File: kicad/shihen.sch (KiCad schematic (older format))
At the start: 51 parts, among them J1 Conn_01x06, J4 USBChargingBoard, Q1 Si1308EDL_NMOS_GSD, Q2 IRLML2502TR(SOT-23, Q_PMOS_GS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, SW1 SW_Push, U1 TPL5110, U2 ESP-12E, U3 ws_epaper_24pin, U4 xc6206p332mr(SOT-23), U5 PCF8563T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

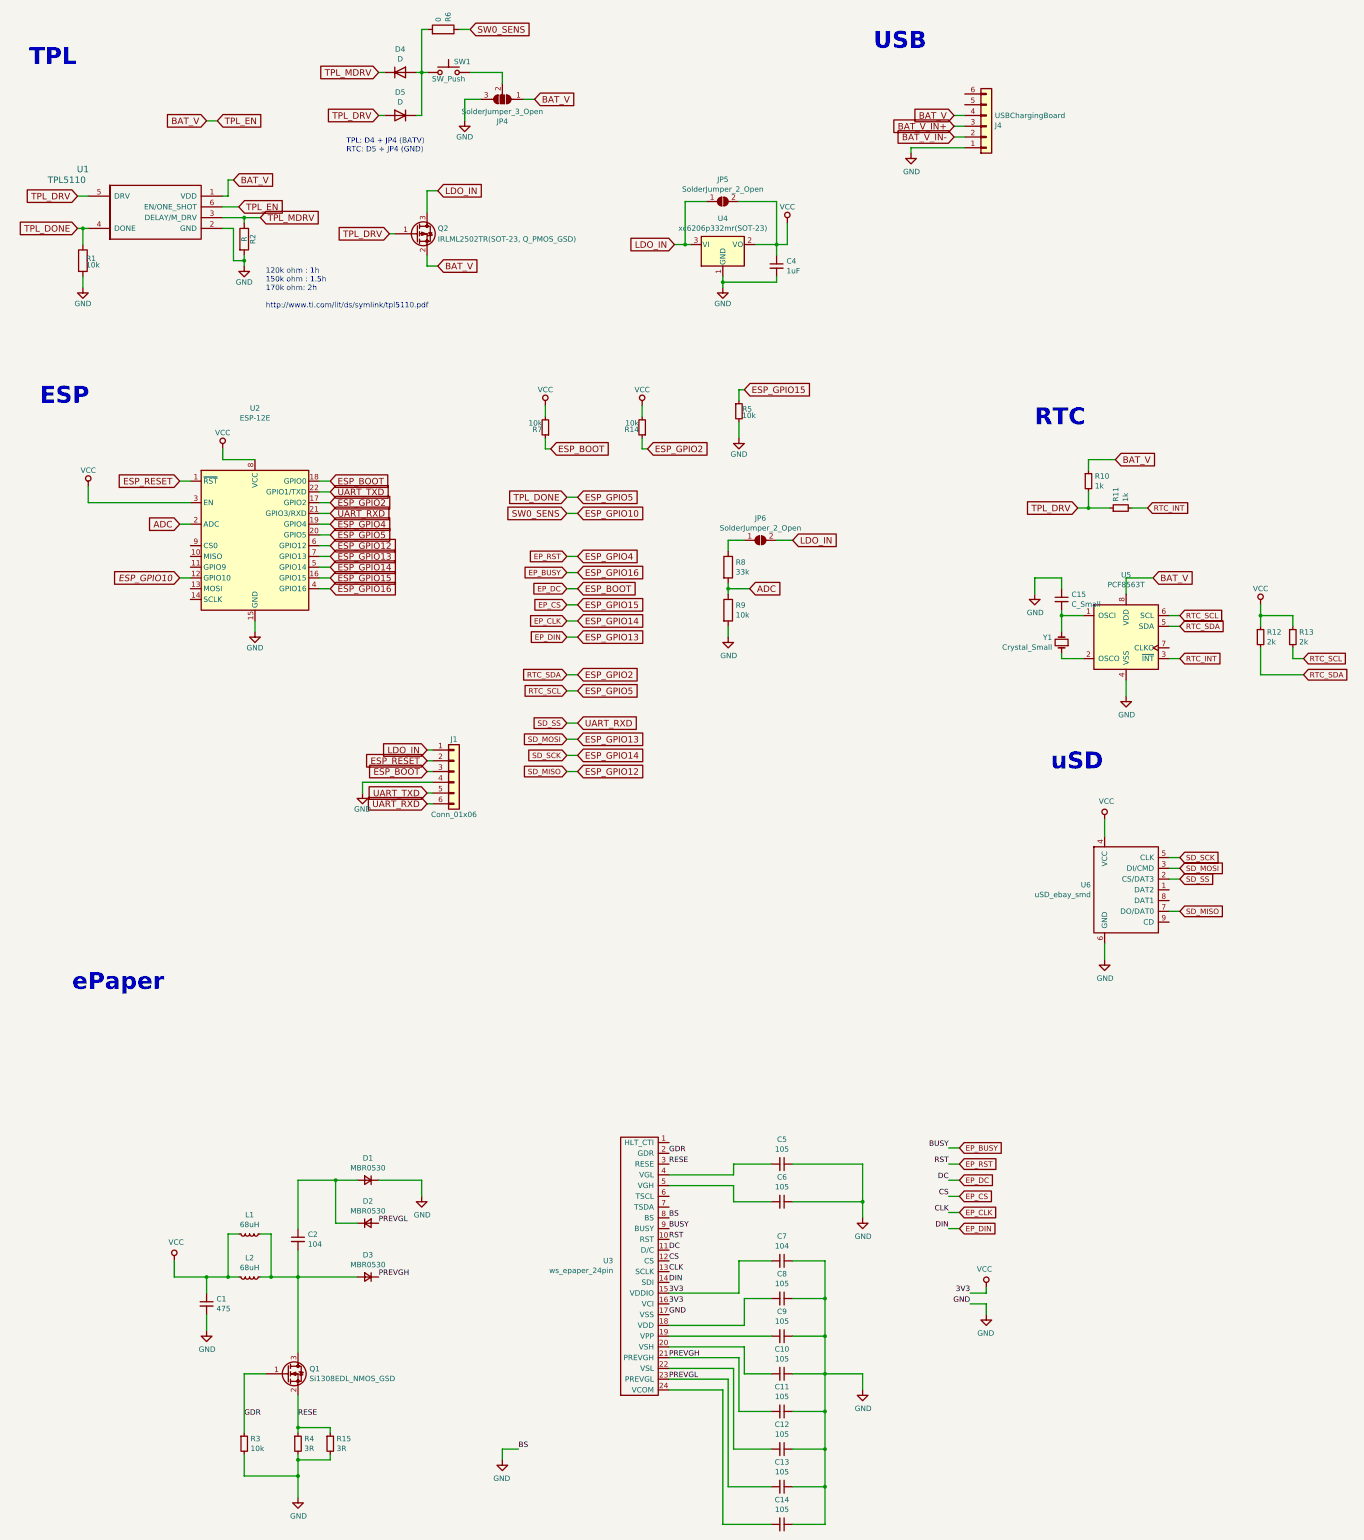
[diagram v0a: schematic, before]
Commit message: Modify schemas - Add MPN(Fusion PCB's part number) as an attribute for PCBA - Fix some wrong constants
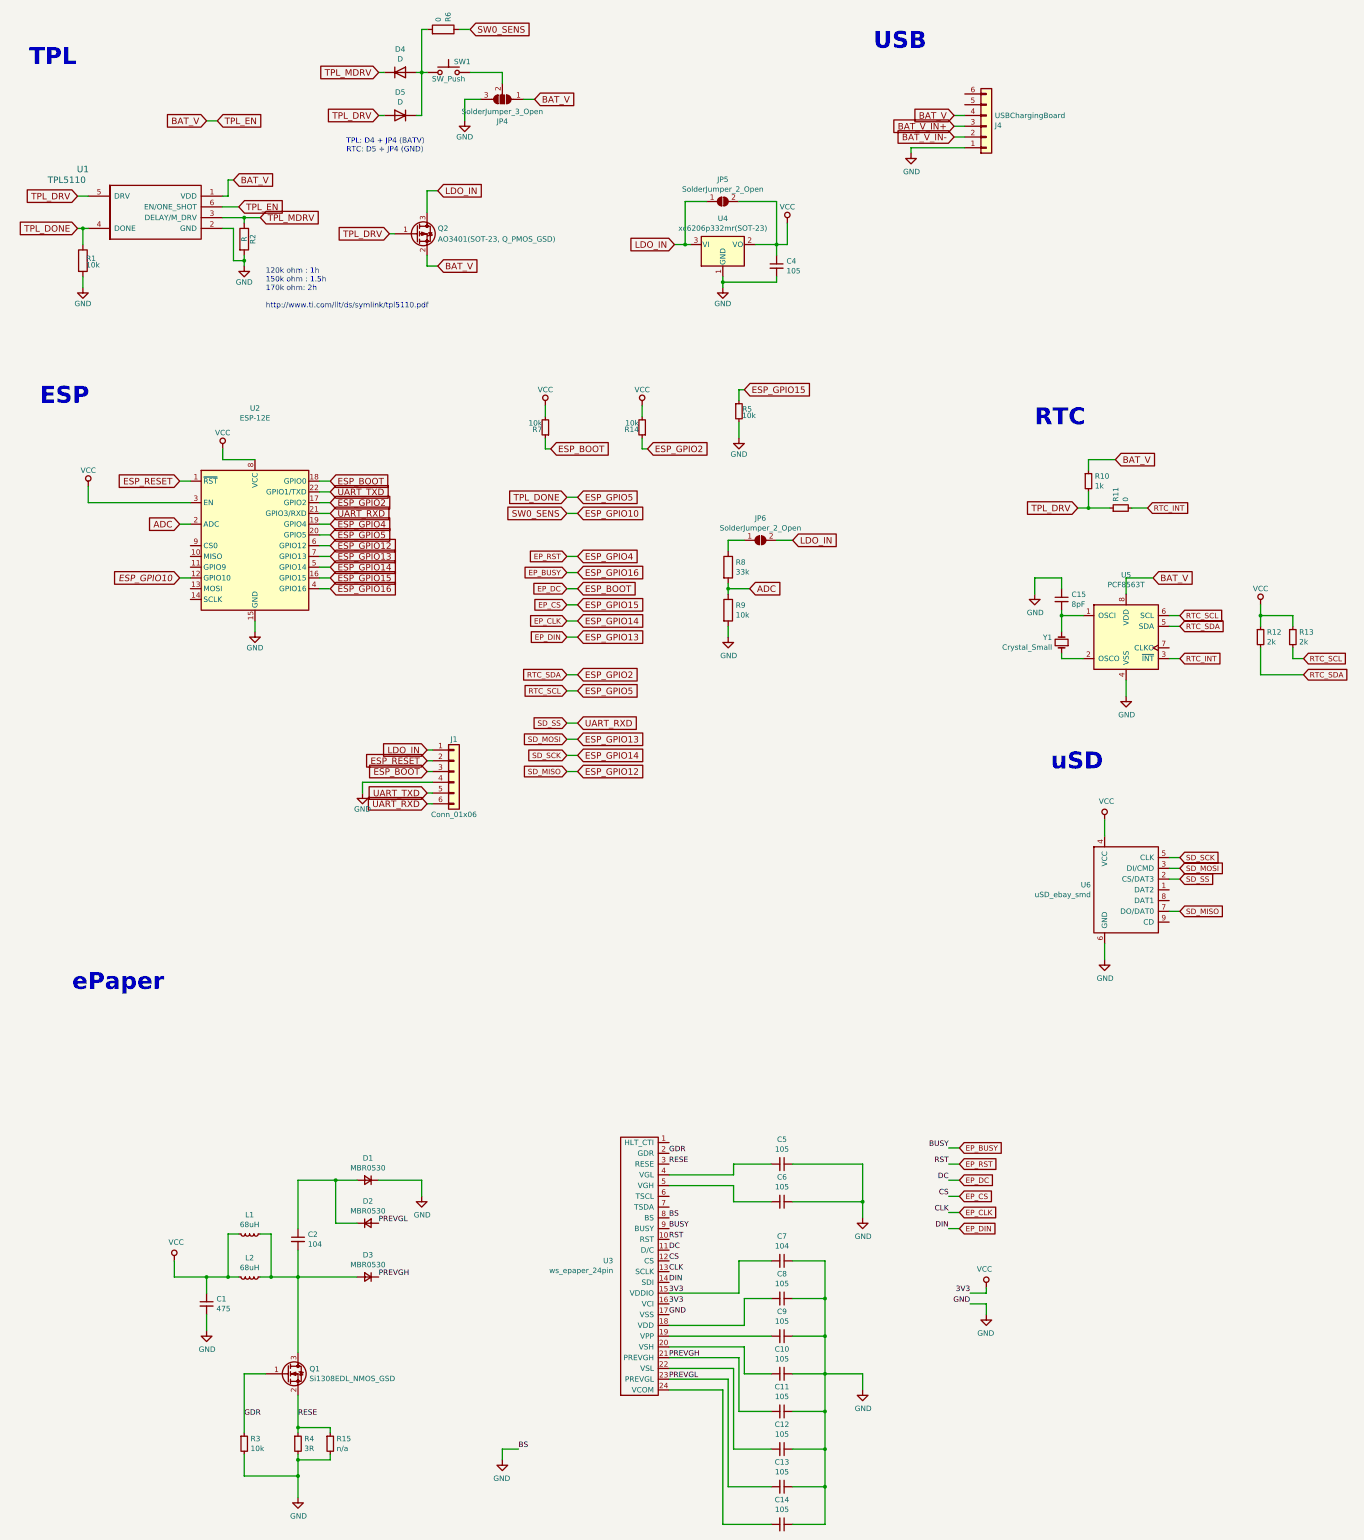
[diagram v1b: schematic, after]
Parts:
- C1: MPN (none) -> CC0805KKX5R8BB475
- C10, C11, C12, C13, C14, C5, C6, C8, C9: MPN (none) -> CC0805KKX7R8BB105
- C15: value C_Small -> 8pF; MPN (none) -> 0805CG8R0C500NT
- C2, C7: MPN (none) -> C0805X104K101T
- C4: value 1uF -> 105; MPN (none) -> CC0805KKX7R8BB105
- D1, D2, D3: MPN (none) -> MBR0530
- D4, D5: MPN (none) -> LL4148ST
- L2: MPN (none) -> NLCV32T-680K-PF
- Q1: MPN_disabled (none) -> SI1308EDL-T1-GE3
- Q2: value IRLML2502TR(SOT-23, Q_PMOS_GSD) -> AO3401(SOT-23, Q_PMOS_GSD); MPN (none) -> CJ2305
- R1, R14, R3, R5, R7, R9: MPN (none) -> RC0805FR-0710KL
- R10: MPN (none) -> RC0805JR-071KL
- R11: value 1k -> 0; MPN (none) -> RC0805FR-070RL
- R15: value 3R -> n/a
- R4: MPN (none) -> 0805W8F300KT5E
- R6: MPN (none) -> RC0805FR-070RL
- R8: MPN (none) -> RC0805FR-0733KL
- U2: MPN (none) -> ESP-12E
- U3: MPN (none) -> FH12A-24S-0.5SH(55)
- U4: MPN (none) -> XC6206P332MR-G
- U5: MPN_disabled (none) -> PCF8563T/5,518
- U6: MPN (none) -> TF-01
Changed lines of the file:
@@
 F 2 "Capacitor_SMD:C_0805_2012Metric_Pad1.15x1.40mm_HandSolder" H 8500 11650 50  0001 C CNN
 F 3 "~" H 8500 11650 50  0001 C CNN
+F 4 "CC0805KKX7R8BB105" H 0   0   50  0001 C CNN "MPN"
 	1    8500 11650
 	0    1    1    0
@@
 F 2 "Capacitor_SMD:C_0805_2012Metric_Pad1.15x1.40mm_HandSolder" H 8500 12000 50  0001 C CNN
 F 3 "~" H 8500 12000 50  0001 C CNN
+F 4 "CC0805KKX7R8BB105" H 0   0   50  0001 C CNN "MPN"
 	1    8500 12000
 	0    1    1    0
@@
 F 2 "Capacitor_SMD:C_0805_2012Metric_Pad1.15x1.40mm_HandSolder" H 8500 12550 50  0001 C CNN
 F 3 "~" H 8500 12550 50  0001 C CNN
+F 4 "C0805X104K101T" H 0   0   50  0001 C CNN "MPN"
 	1    8500 12550
 	0    1    1    0
@@
 F 2 "Capacitor_SMD:C_0805_2012Metric_Pad1.15x1.40mm_HandSolder" H 8500 12900 50  0001 C CNN
 F 3 "~" H 8500 12900 50  0001 C CNN
+F 4 "CC0805KKX7R8BB105" H 0   0   50  0001 C CNN "MPN"
 	1    8500 12900
 	0    1    1    0
@@
 F 2 "Capacitor_SMD:C_0805_2012Metric_Pad1.15x1.40mm_HandSolder" H 8500 13250 50  0001 C CNN
 F 3 "~" H 8500 13250 50  0001 C CNN
+F 4 "CC0805KKX7R8BB105" H 0   0   50  0001 C CNN "MPN"
 	1    8500 13250
 	0    1    1    0
@@
 F 2 "Capacitor_SMD:C_0805_2012Metric_Pad1.15x1.40mm_HandSolder" H 8500 13600 50  0001 C CNN
 F 3 "~" H 8500 13600 50  0001 C CNN
+F 4 "CC0805KKX7R8BB105" H 0   0   50  0001 C CNN "MPN"
 	1    8500 13600
 	0    1    1    0
@@
 F 2 "Capacitor_SMD:C_0805_2012Metric_Pad1.15x1.40mm_HandSolder" H 8500 13950 50  0001 C CNN
 F 3 "~" H 8500 13950 50  0001 C CNN
+F 4 "CC0805KKX7R8BB105" H 0   0   50  0001 C CNN "MPN"
 	1    8500 13950
 	0    1    1    0
@@
 F 2 "Capacitor_SMD:C_0805_2012Metric_Pad1.15x1.40mm_HandSolder" H 8500 14300 50  0001 C CNN
 F 3 "~" H 8500 14300 50  0001 C CNN
+F 4 "CC0805KKX7R8BB105" H 0   0   50  0001 C CNN "MPN"
 	1    8500 14300
 	0    1    1    0
@@
 F 2 "Capacitor_SMD:C_0805_2012Metric_Pad1.15x1.40mm_HandSolder" H 8500 14650 50  0001 C CNN
 F 3 "~" H 8500 14650 50  0001 C CNN
+F 4 "CC0805KKX7R8BB105" H 0   0   50  0001 C CNN "MPN"
 	1    8500 14650
 	0    1    1    0
@@
 F 2 "Capacitor_SMD:C_0805_2012Metric_Pad1.15x1.40mm_HandSolder" H 8500 15000 50  0001 C CNN
 F 3 "~" H 8500 15000 50  0001 C CNN
+F 4 "CC0805KKX7R8BB105" H 0   0   50  0001 C CNN "MPN"
 	1    8500 15000
 	0    1    1    0
@@
 F 2 "Connector_FFC-FPC:Hirose_FH12-24S-0.5SH_1x24-1MP_P0.50mm_Horizontal_reverse" H 7350 11250 50  0001 C CNN
 F 3 "" H 7350 11250 50  0001 C CNN
+F 4 "FH12A-24S-0.5SH(55)" H 0   0   50  0001 C CNN "MPN"
 	1    7350 11250
 	-1   0    0    -1
@@
 F 2 "Diode_SMD:D_SOD-123" V 4650 11800 50  0001 C CNN
 F 3 "~" V 4650 11800 50  0001 C CNN
+F 4 "MBR0530" H 0   0   50  0001 C CNN "MPN"
 	1    4650 11800
 	-1   0    0    1
@@
 F 2 "Diode_SMD:D_SOD-123" V 4650 12200 50  0001 C CNN
 F 3 "~" V 4650 12200 50  0001 C CNN
+F 4 "MBR0530" H 0   0   50  0001 C CNN "MPN"
 	1    4650 12200
 	1    0    0    1
@@
 F 2 "Diode_SMD:D_SOD-123" V 4650 12700 50  0001 C CNN
 F 3 "~" V 4650 12700 50  0001 C CNN
+F 4 "MBR0530" H 0   0   50  0001 C CNN "MPN"
 	1    4650 12700
 	-1   0    0    1
@@
 F 2 "Capacitor_SMD:C_0805_2012Metric_Pad1.15x1.40mm_HandSolder" H 4000 12350 50  0001 C CNN
 F 3 "~" H 4000 12350 50  0001 C CNN
+F 4 "C0805X104K101T" H 0   0   50  0001 C CNN "MPN"
 	1    4000 12350
 	1    0    0    -1
@@
 F 2 "Inductor_SMD:L_1206_3216Metric_Pad1.42x1.75mm_HandSolder" H 3550 12700 50  0001 C CNN
 F 3 "~" H 3550 12700 50  0001 C CNN
+F 4 "NLCV32T-680K-PF" H 0   0   50  0001 C CNN "MPN"
 	1    3550 12700
 	0    1    1    0
@@
 F 2 "Capacitor_SMD:C_0805_2012Metric_Pad1.15x1.40mm_HandSolder" H 3150 12950 50  0001 C CNN
 F 3 "~" H 3150 12950 50  0001 C CNN
+F 4 "CC0805KKX5R8BB475" H 0   0   50  0001 C CNN "MPN"
 	1    3150 12950
 	1    0    0    -1
@@
 F 2 "Package_TO_SOT_SMD:SOT-323_SC-70_Handsoldering" H 4100 13700 50  0001 C CNN
 F 3 "~" H 3900 13600 50  0001 C CNN
+F 4 "SI1308EDL-T1-GE3" H 0   0   50  0001 C CNN "MPN_disabled"
 	1    3900 13600
 	1    0    0    -1
@@
 F 2 "Resistor_SMD:R_0805_2012Metric" H 4000 14250 50  0001 C CNN
 F 3 "~" H 4000 14250 50  0001 C CNN
+F 4 "0805W8F300KT5E" H 0   0   50  0001 C CNN "MPN"
 	1    4000 14250
 	1    0    0    -1
@@
 F 2 "Resistor_SMD:R_0805_2012Metric" H 3500 14250 50  0001 C CNN
 F 3 "~" H 3500 14250 50  0001 C CNN
+F 4 "RC0805FR-0710KL" H 0   0   50  0001 C CNN "MPN"
 	1    3500 14250
 	1    0    0    -1
@@
 F 2 "Resistor_SMD:R_0805_2012Metric" H 8100 4650 50  0001 C CNN
 F 3 "" H 8100 4650 50  0001 C CNN
+F 4 "RC0805FR-0710KL" H 0   0   50  0001 C CNN "MPN"
 	1    8100 4650
 	1    0    0    -1
@@
 F 2 "Resistor_SMD:R_0805_2012Metric" H 6300 4800 50  0001 C CNN
 F 3 "" H 6300 4800 50  0001 C CNN
+F 4 "RC0805FR-0710KL" H 0   0   50  0001 C CNN "MPN"
 	1    6300 4800
 	-1   0    0    1
@@
 P 5100 3000
 F 0 "Q2" H 5300 3050 50  0000 L CNN
-F 1 "IRLML2502TR(SOT-23, Q_PMOS_GSD)" H 5300 2950 50  0000 L CNN
+F 1 "AO3401(SOT-23, Q_PMOS_GSD)" H 5300 2950 50  0000 L CNN
 F 2 "Package_TO_SOT_SMD:SOT-23_Handsoldering" H 5300 3100 50  0001 C CNN
 F 3 "" H 5100 3000 50  0001 C CNN
+F 4 "CJ2305" H 0   0   50  0001 C CNN "MPN"
 	1    5100 3000
 	1    0    0    -1
@@
 F 2 "Resistor_SMD:R_0805_2012Metric" H 2000 3250 50  0001 C CNN
 F 3 "" H 2000 3250 50  0001 C CNN
+F 4 "RC0805FR-0710KL" H 0   0   50  0001 C CNN "MPN"
 	1    2000 3250
 	1    0    0    -1
@@
 P 8450 3300
 F 0 "C4" H 8542 3346 50  0000 L CNN
-F 1 "1uF" H 8542 3255 50  0000 L CNN
+F 1 "105" H 8542 3255 50  0000 L CNN
 F 2 "Capacitor_SMD:C_0805_2012Metric_Pad1.15x1.40mm_HandSolder" H 8450 3300 50  0001 C CNN
 F 3 "~" H 8450 3300 50  0001 C CNN
+F 4 "CC0805KKX7R8BB105" H 0   0   50  0001 C CNN "MPN"
 	1    8450 3300
 	1    0    0    -1
@@
 F 2 "Package_TO_SOT_SMD:SOT-23_Handsoldering" H 7950 3300 50  0001 C CNN
 F 3 "http://www.diodes.com/datasheets/AP1117.pdf" H 8050 2850 50  0001 C CNN
+F 4 "XC6206P332MR-G" H 0   0   50  0001 C CNN "MPN"
 	1    7950 3100
 	1    0    0    -1
@@
 F 2 "lib_ext:ESP-12E" H 3600 6150 50  0001 C CNN
 F 3 "http://wiki.ai-thinker.com/_media/esp8266/docs/aithinker_esp_12f_datasheet_en.pdf" H 3250 6200 50  0001 C CNN
+F 4 "ESP-12E" H 3600 5900 50  0001 C CNN "MPN"
 	1    3600 5900
 	1    0    0    -1
@@
 F 2 "Resistor_SMD:R_0805_2012Metric" V 7930 6100 50  0001 C CNN
 F 3 "~" H 8000 6100 50  0001 C CNN
+F 4 "RC0805FR-0733KL" H 0   0   50  0001 C CNN "MPN"
 	1    8000 6100
 	1    0    0    -1
@@
 F 2 "Resistor_SMD:R_0805_2012Metric" V 7930 6500 50  0001 C CNN
 F 3 "~" H 8000 6500 50  0001 C CNN
+F 4 "RC0805FR-0710KL" H 0   0   50  0001 C CNN "MPN"
 	1    8000 6500
 	1    0    0    -1
@@
 F 2 "Diode_SMD:D_1206_3216Metric_Pad1.42x1.75mm_HandSolder" H 4950 1500 50  0001 C CNN
 F 3 "~" H 4950 1500 50  0001 C CNN
+F 4 "LL4148ST" H 0   0   50  0001 C CNN "MPN"
 	1    4950 1500
 	1    0    0    -1
@@
 F 2 "Resistor_SMD:R_0805_2012Metric" V 5280 1100 50  0001 C CNN
 F 3 "~" H 5350 1100 50  0001 C CNN
+F 4 "RC0805FR-070RL" H 0   0   50  0001 C CNN "MPN"
 	1    5350 1100
 	0    1    -1   0
@@
 F 2 "Package_SO:SOIC-8_3.9x4.9mm_P1.27mm" H 11700 6750 50  0001 C CNN
 F 3 "http://www.nxp.com/documents/data_sheet/PCF8563.pdf" H 11700 6750 50  0001 C CNN
+F 4 "PCF8563T/5,518" H 0   0   50  0001 C CNN "MPN_disabled"
 	1    11700 6750
 	1    0    0    -1
@@
 P 11100 6400
 F 0 "C15" H 11192 6446 50  0000 L CNN
-F 1 "C_Small" H 11192 6355 50  0000 L CNN
+F 1 "8pF" H 11192 6355 50  0000 L CNN
 F 2 "Capacitor_SMD:C_0805_2012Metric_Pad1.15x1.40mm_HandSolder" H 11100 6400 50  0001 C CNN
 F 3 "~" H 11100 6400 50  0001 C CNN
+F 4 "0805CG8R0C500NT" H 0   0   50  0001 C CNN "MPN"
 	1    11100 6400
 	1    0    0    -1
@@
 F 2 "Resistor_SMD:R_0805_2012Metric" H 11350 5300 50  0001 C CNN
 F 3 "~" H 11350 5300 50  0001 C CNN
+F 4 "RC0805JR-071KL" H 0   0   50  0001 C CNN "MPN"
 	1    11350 5300
 	1    0    0    -1
@@
 P 11650 5550
 F 0 "R11" H 11709 5596 50  0000 L CNN
-F 1 "1k" H 11709 5505 50  0000 L CNN
+F 1 "0" H 11709 5505 50  0000 L CNN
 F 2 "Resistor_SMD:R_0805_2012Metric" H 11650 5550 50  0001 C CNN
 F 3 "~" H 11650 5550 50  0001 C CNN
+F 4 "RC0805FR-070RL" H 0   0   50  0001 C CNN "MPN"
 	1    11650 5550
 	0    -1   -1   0
@@
 F 2 "Diode_SMD:D_1206_3216Metric_Pad1.42x1.75mm_HandSolder" H 4950 1900 50  0001 C CNN
 F 3 "~" H 4950 1900 50  0001 C CNN
+F 4 "LL4148ST" H 0   0   50  0001 C CNN "MPN"
 	1    4950 1900
 	-1   0    0    -1
@@
 F 2 "Resistor_SMD:R_0805_2012Metric" H 7200 4800 50  0001 C CNN
 F 3 "" H 7200 4800 50  0001 C CNN
+F 4 "RC0805FR-0710KL" H 0   0   50  0001 C CNN "MPN"
 	1    7200 4800
 	-1   0    0    1
@@
 P 4300 14250
 F 0 "R15" H 4359 14296 50  0000 L CNN
-F 1 "3R" H 4359 14205 50  0000 L CNN
+F 1 "n/a" H 4359 14205 50  0000 L CNN
 F 2 "Resistor_SMD:R_0805_2012Metric" H 4300 14250 50  0001 C CNN
 F 3 "~" H 4300 14250 50  0001 C CNN
+F 4 "" H 0   0   50  0001 C CNN "MPN"
 	1    4300 14250
 	1    0    0    -1
@@
 F 2 "lib_ext:Conn_uSDcard" H 11350 8550 50  0001 C CNN
 F 3 "" H 11350 8550 50  0001 C CNN
+F 4 "TF-01" H 0   0   50  0001 C CNN "MPN"
 	1    11350 8550
 	1    0    0    -1
